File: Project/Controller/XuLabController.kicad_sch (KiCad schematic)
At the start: 4 parts

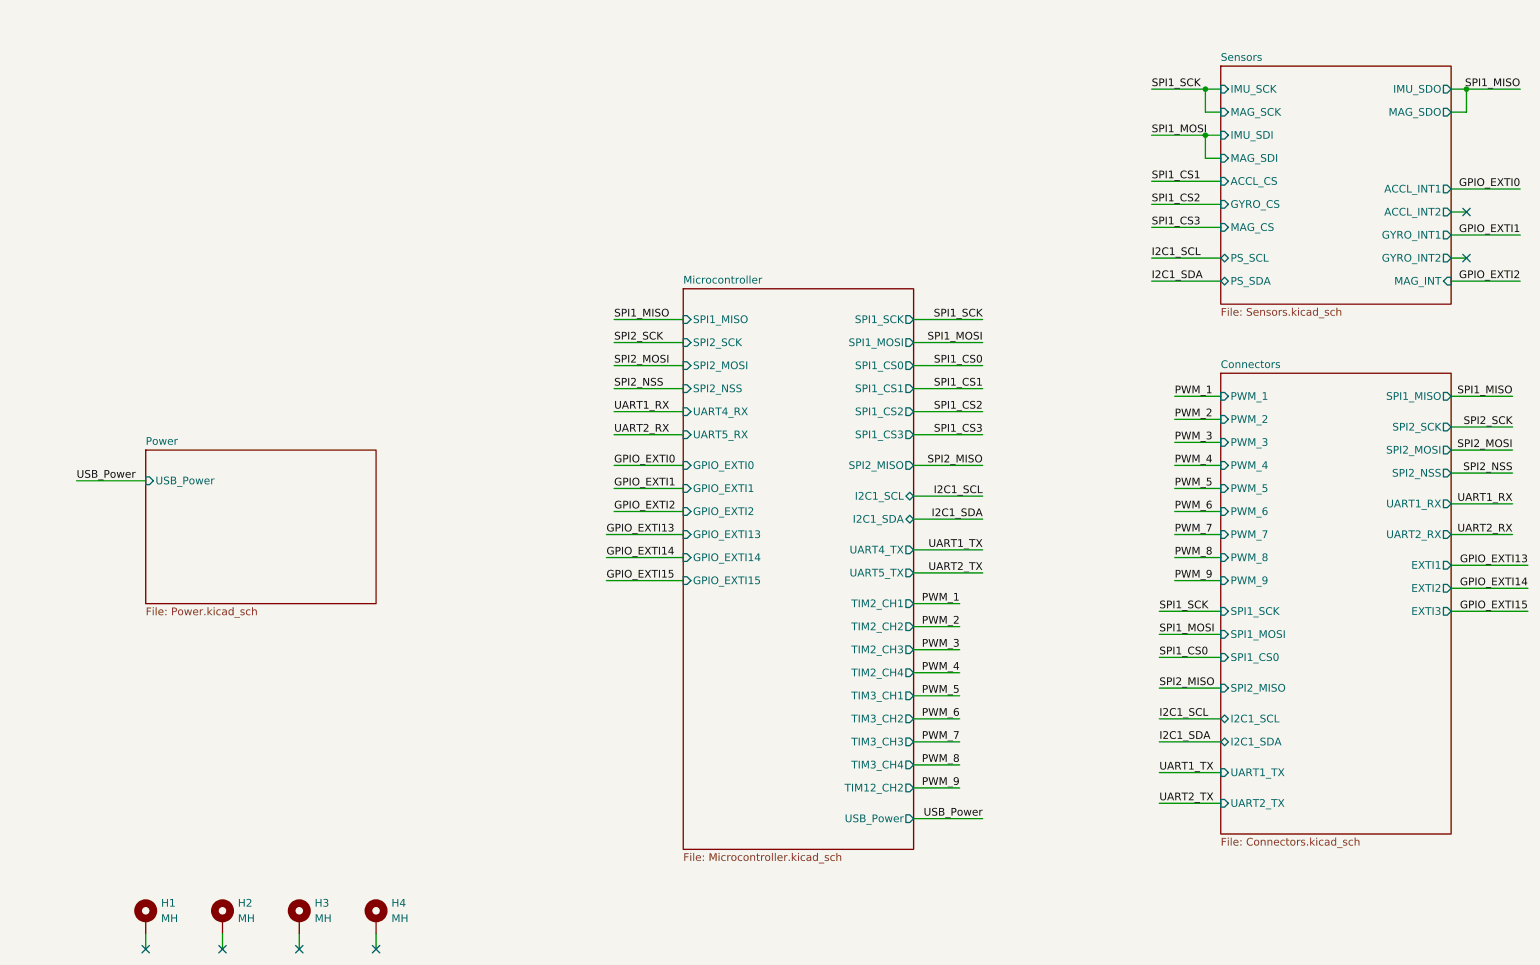
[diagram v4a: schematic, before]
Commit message: Add MCP9700A temperature sensor
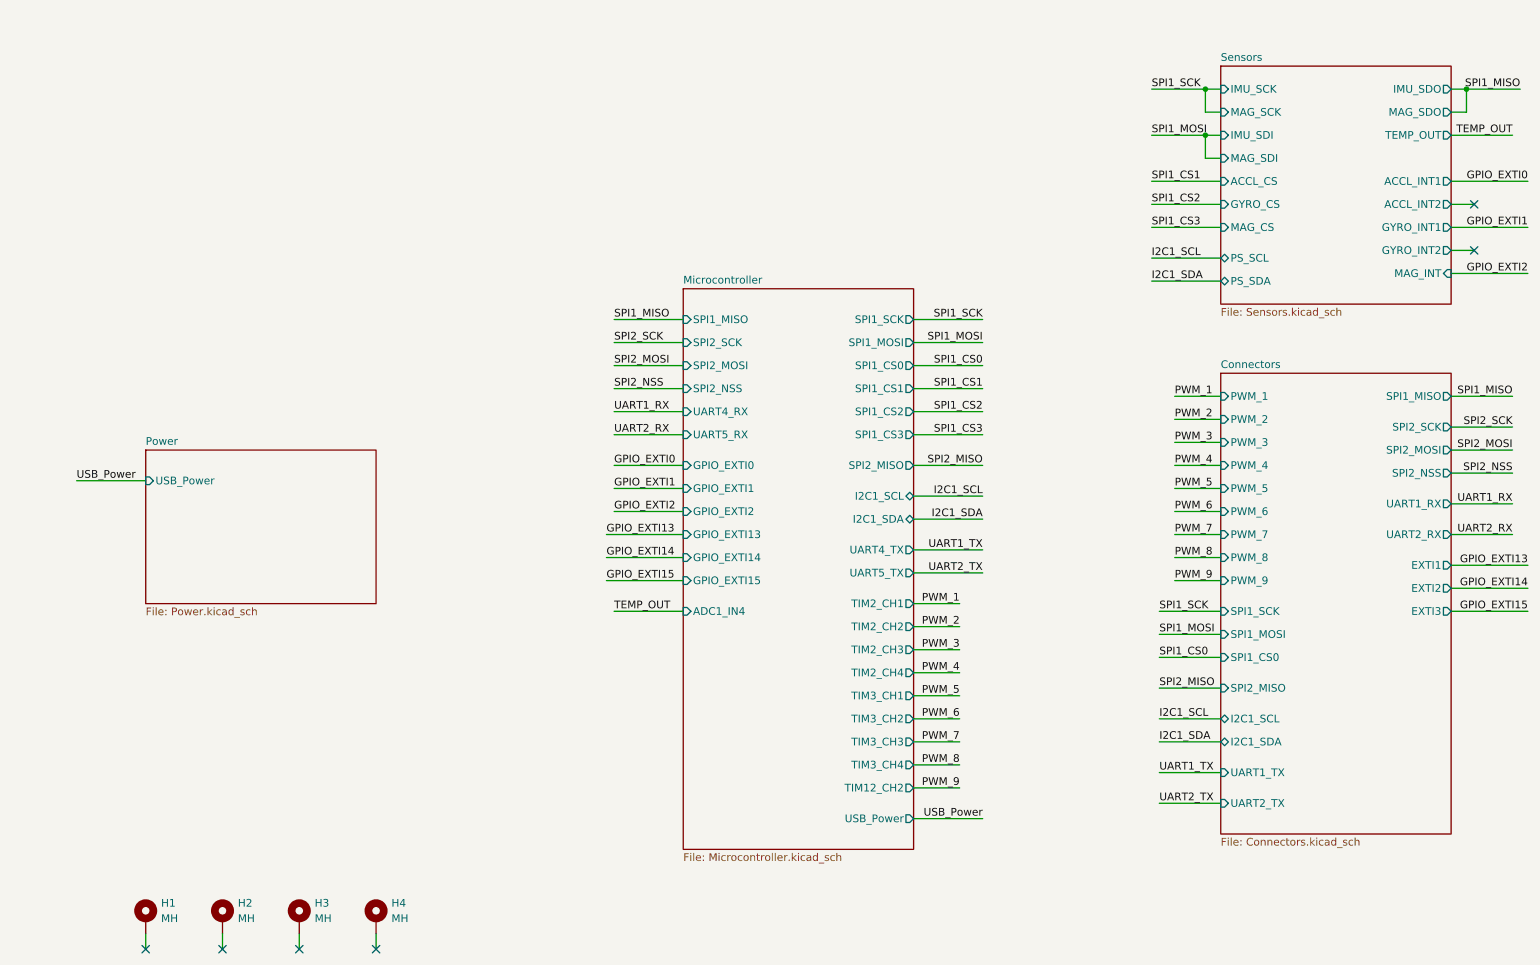
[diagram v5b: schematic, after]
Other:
- sheet Microcontroller ports: added ADC1_IN4; removed none
- sheet Sensors ports: added TEMP_OUT; removed none
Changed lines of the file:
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@@
 	(title_block
 		(title "Main Sheet")
-		(date "2026-02-05")
+		(date "2026-02-10")
 		(rev "B")
 		(company "CU Boulder Senior Design Team 29 - Xu Lab")
@@
 	)
 	(no_connect
-		(at 256.54 49.53)
+		(at 257.81 48.26)
 	)
 	(no_connect
@@
 	)
 	(no_connect
-		(at 256.54 57.15)
+		(at 257.81 55.88)
 	)
 	(wire
@@
 	(wire
 		(pts
+			(xy 254 36.83) (xy 264.16 36.83)
+		)
+		(stroke
+			(width 0)
+			(type default)
+		)
+	)
+	(wire
+		(pts
 			(xy 165.1 91.44) (xy 176.53 91.44)
 		)
@@
 	(wire
 		(pts
-			(xy 254 53.34) (xy 265.43 53.34)
+			(xy 254 52.07) (xy 266.7 52.07)
 		)
 		(stroke
@@
 	(wire
 		(pts
-			(xy 254 60.96) (xy 265.43 60.96)
+			(xy 254 59.69) (xy 266.7 59.69)
 		)
 		(stroke
@@
 	(wire
 		(pts
-			(xy 254 49.53) (xy 256.54 49.53)
+			(xy 254 48.26) (xy 257.81 48.26)
 		)
 		(stroke
@@
 	(wire
 		(pts
-			(xy 254 57.15) (xy 256.54 57.15)
+			(xy 115.57 115.57) (xy 127 115.57)
+		)
+		(stroke
+			(width 0)
+			(type default)
+		)
+	)
+	(wire
+		(pts
+			(xy 254 55.88) (xy 257.81 55.88)
 		)
 		(stroke
@@
 	(wire
 		(pts
-			(xy 254 45.72) (xy 265.43 45.72)
+			(xy 254 44.45) (xy 266.7 44.45)
 		)
 		(stroke
@@
 		)
 	)
+	(label "TEMP_OUT"
+		(at 264.16 36.83 180)
+		(effects
+			(font
+				(size 1.27 1.27)
+			)
+			(justify right bottom)
+		)
+	)
 	(label "PWM_8"
 		(at 172.72 140.97 180)
@@
 		)
 	)
+	(label "TEMP_OUT"
+		(at 115.57 115.57 0)
+		(effects
+			(font
+				(size 1.27 1.27)
+			)
+			(justify left bottom)
+		)
+	)
 	(label "PWM_1"
 		(at 172.72 114.3 180)
@@
 	)
 	(label "GPIO_EXTI2"
-		(at 265.43 60.96 180)
+		(at 266.7 59.69 180)
 		(effects
 			(font
@@
 	)
 	(label "GPIO_EXTI0"
-		(at 265.43 45.72 180)
+		(at 266.7 44.45 180)
 		(effects
 			(font
@@
 	)
 	(label "GPIO_EXTI1"
-		(at 265.43 53.34 180)
+		(at 266.7 52.07 180)
 		(effects
 			(font
@@
 			)
 		)
+		(pin "ADC1_IN4" input
+			(at 127 115.57 180)
+			(effects
+				(font
+					(size 1.27 1.27)
+				)
+				(justify left)
+			)
+		)
 		(instances
 			(project "XuLabController"
@@
 		)
 		(pin "ACCL_INT1" output
-			(at 254 45.72 0)
+			(at 254 44.45 0)
 			(effects
 				(font
@@
 		)
 		(pin "ACCL_INT2" output
-			(at 254 49.53 0)
+			(at 254 48.26 0)
 			(effects
 				(font
@@
 		)
 		(pin "GYRO_INT1" output
-			(at 254 53.34 0)
+			(at 254 52.07 0)
 			(effects
 				(font
@@
 		)
 		(pin "GYRO_INT2" output
-			(at 254 57.15 0)
+			(at 254 55.88 0)
 			(effects
 				(font
@@
 		)
 		(pin "MAG_INT" input
-			(at 254 60.96 0)
-			(effects
-				(font
+			(at 254 59.69 0)
+			(effects
+				(font
+					(size 1.27 1.27)
+				)
+				(justify right)
+			)
+		)
+		(pin "TEMP_OUT" output
+			(at 254 36.83 0)
+			(effects
+				(font
